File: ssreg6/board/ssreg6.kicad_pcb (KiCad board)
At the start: 2 copper layers, 48 x 86 mm, 76 parts, among them J1 PROG, J2 AUX, U2 FR8205, U3 ESP32-C3-WROOM-02, U4 LM358, U5 LM358, U6 LM358, U7 LTV-354T, X1 12V, X2 TARIFF

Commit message: board design
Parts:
- moved R2 1.50 mm to (133.5, 56.5)
- moved X2 1.09 mm to (151.7, 37.7)
- moved X1 1.09 mm to (144.0, 37.7)
- moved D1 1.00 mm to (133.0, 52.0)
- moved DO1 1.00 mm to (116.2, 106.7)
- moved I2C1 1.00 mm to (144.7, 106.7)
- moved R38 1.00 mm to (129.0, 52.0)
- moved C3 0.50 mm to (133.5, 59.0), turned to 0 degrees
- moved R4 0.50 mm to (138.0, 55.5)
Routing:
- net GND: track 43.6 -> 46.8 mm, vias 96 -> 101
- net Net-(U2-SHDN): track 4.03 -> 3.00 mm
- net /SCL: track 91.5 -> 92.5 mm
- net /AOUT4: track 21.0 -> 22.0 mm
- net /AOUT2: track 34.6 -> 35.6 mm
- net /AOUT1: track 57.0 -> 58.0 mm
- net /AOUT0: track 48.5 -> 49.5 mm
- net /AOUT3: track 42.5 -> 43.5 mm
- net +12V: track 79.4 -> 80.0 mm
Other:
- outline, holes or cut-outs redrawn
- board text removed: "-"

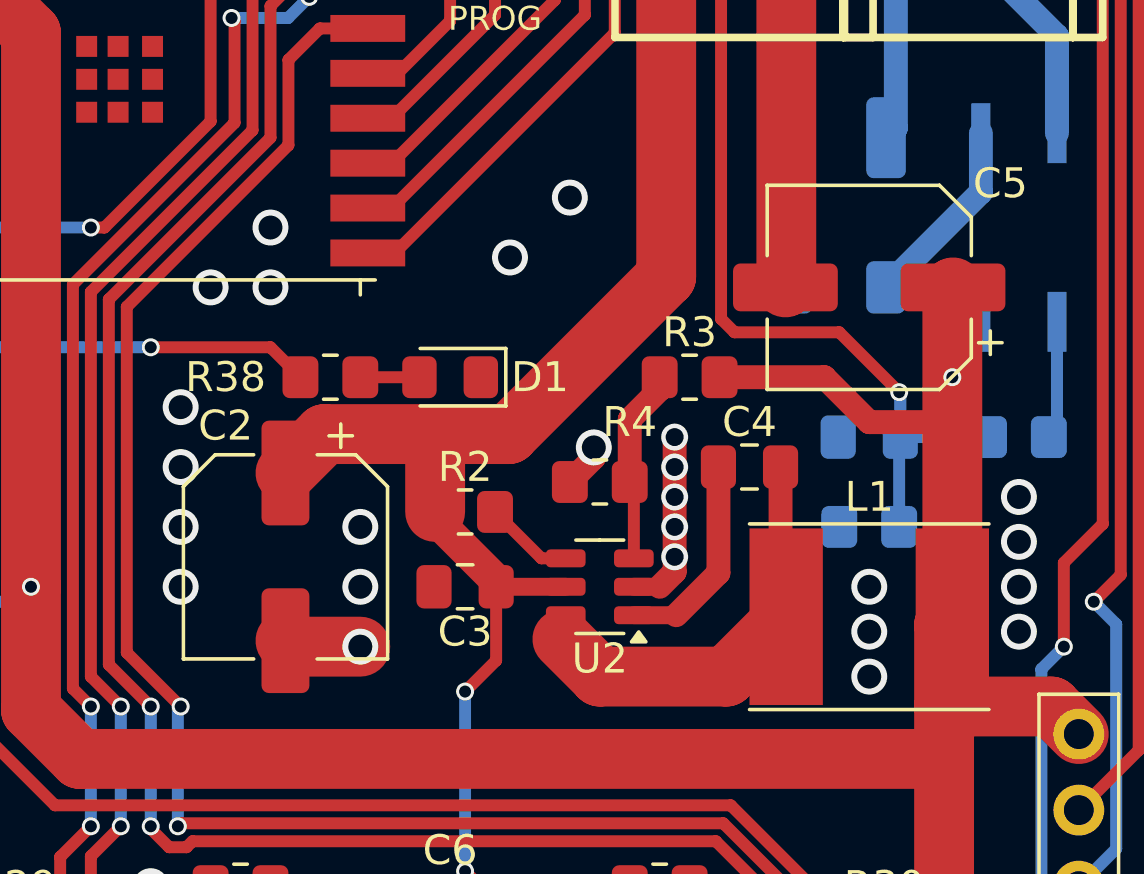
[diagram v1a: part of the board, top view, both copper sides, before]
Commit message: ceramic capacitors on PSU & JLC order
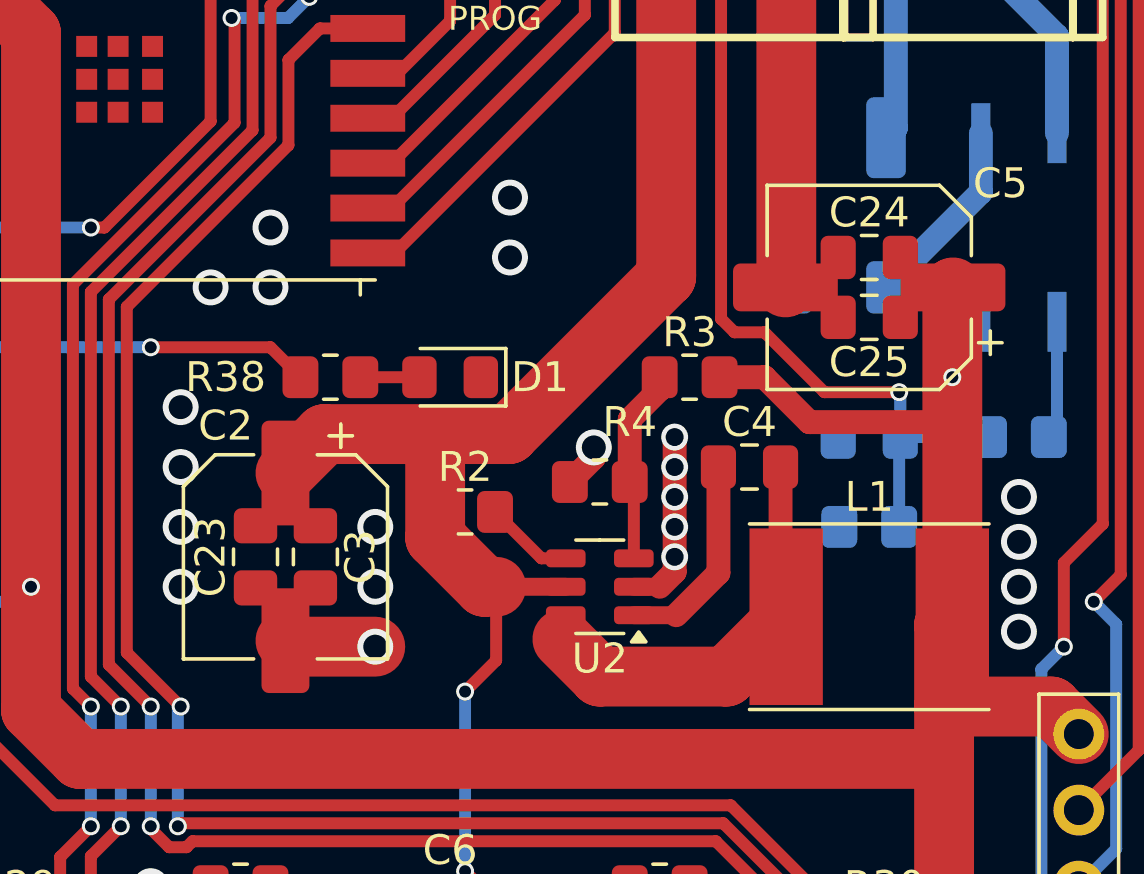
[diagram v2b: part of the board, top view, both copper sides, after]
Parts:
- added C23: 10u/16V, Capacitor_SMD:C_0805_2012Metric_Pad1.18x1.45mm_HandSolder, F.Cu at (126.5, 58.0)
- added C24: 10u/16V, Capacitor_SMD:C_0805_2012Metric_Pad1.18x1.45mm_HandSolder, F.Cu at (147.0, 48.0)
- added C25: 10u/16V, Capacitor_SMD:C_0805_2012Metric_Pad1.18x1.45mm_HandSolder, F.Cu at (147.0, 50.0)
- C3: value 100n -> 10u/16V
- C5: value 100u/12V -> 100u/16V
- moved C3 5.10 mm to (128.5, 58.0), turned to -90 degrees
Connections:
- C3 pad 1: GND -> +12V
- C3 pad 2: +12V -> GND
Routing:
- net GND: track 46.8 -> 47.3 mm, vias 101 -> 98
